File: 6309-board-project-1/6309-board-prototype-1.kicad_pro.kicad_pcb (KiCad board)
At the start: 2 copper layers, 100 x 140 mm, 35 parts, among them J1 PWR, J2 FTDI, SW1 B3F-1000, U1 63C09, U2 62256, U3 39FS010, U4 16550, U5 74HCT04, U6 74HCT32, U7 74HCT30, X1 12MHz, X2 1.8432 MHz

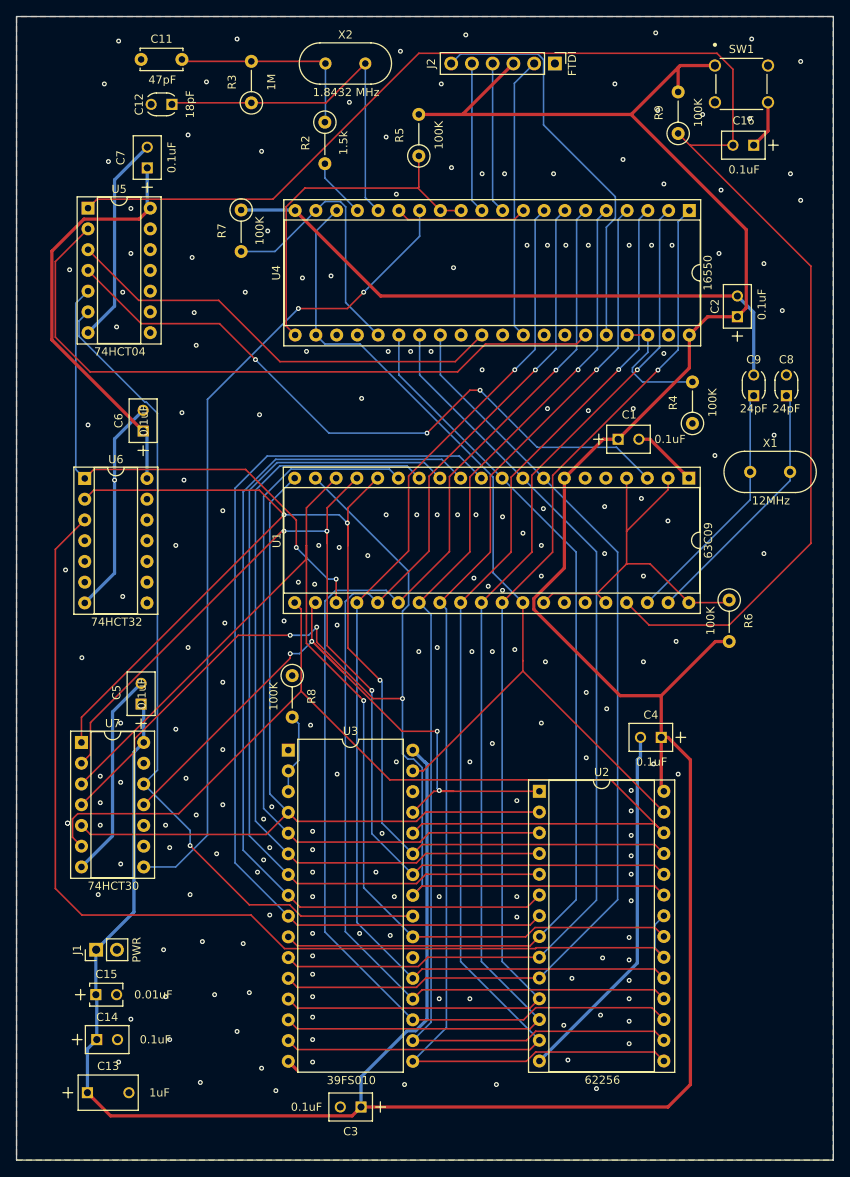
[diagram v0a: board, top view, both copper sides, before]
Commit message: remove excess vias
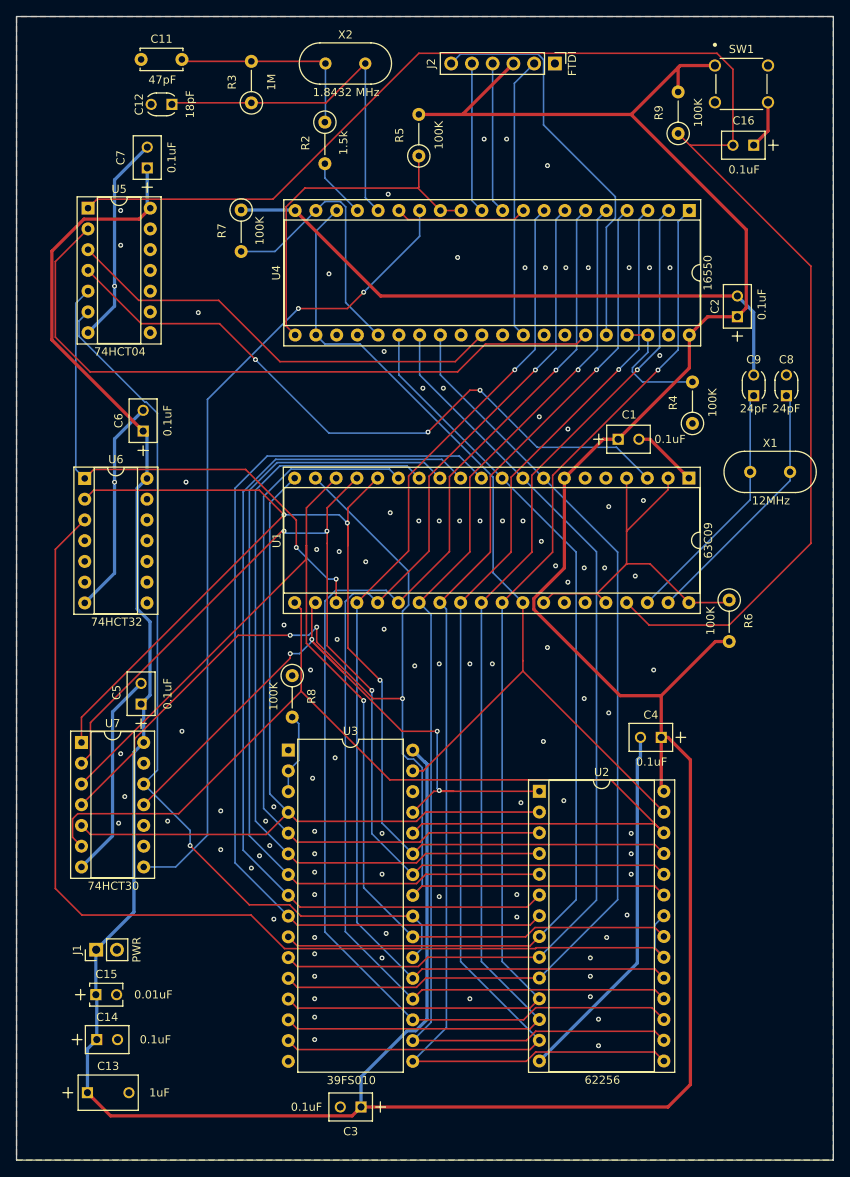
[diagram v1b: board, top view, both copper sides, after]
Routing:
- net +5V: track 446.2 -> 475.4 mm
- net /!A15: track 103.8 -> 109.8 mm
- net GND: track 213.7 -> 212.2 mm, vias 201 -> 101
- net /A9: track 131.7 -> 130.4 mm
- net /A5: vias 0 -> 1

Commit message: fix DRC errors
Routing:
- net /A14: track 85.1 -> 86.3 mm
- net GND: vias 101 -> 105
- net /A5: vias 1 -> 0
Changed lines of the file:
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@@
+	)
+	(via
+		(at 58.75 97.25)
+		(size 0.6)
+		(drill 0.3)
+		(layers "F.Cu" "B.Cu")
+		(free yes)
+		(net 2)
 	)
 	(via
@@
 	)
 	(via
+		(at 38.5 53)
+		(size 0.6)
+		(drill 0.3)
+		(layers "F.Cu" "B.Cu")
+		(free yes)
+		(net 2)
+	)
+	(via
 		(at 95.75 81.75)
 		(size 0.6)
@@
 	)
 	(via
+		(at 51.5 104)
+		(size 0.6)
+		(drill 0.3)
+		(layers "F.Cu" "B.Cu")
+		(free yes)
+		(net 2)
+	)
+	(via
 		(at 59 88.75)
 		(size 0.6)
@@
 		(drill 0.3)
 		(layers "F.Cu" "B.Cu")
+		(net 2)
+	)
+	(via
+		(at 46.75 92.5)
+		(size 0.6)
+		(drill 0.3)
+		(layers "F.Cu" "B.Cu")
+		(free yes)
 		(net 2)
 	)
@@
 		(net 18)
 	)
-	(via
-		(at 59.485 119.265)
-		(size 0.6)
-		(drill 0.3)
-		(layers "F.Cu" "B.Cu")
-		(net 18)
-	)
 	(segment
 		(start 59.485 119.265)
@@
 	)
 	(segment
+		(start 57.75 92.25)
+		(end 46.25 103.75)
+		(width 0.2)
+		(layer "F.Cu")
+		(net 32)
+	)
+	(segment
 		(start 78.1 109.1)
 		(end 79.75 109.1)
@@
 	)
 	(segment
+		(start 59.75 92.25)
+		(end 57.75 92.25)
+		(width 0.2)
+		(layer "F.Cu")
+		(net 32)
+	)
+	(segment
 		(start 78 109)
 		(end 78.1 109.1)
@@
 	)
 	(segment
-		(start 59.75 92.815)
-		(end 59.75 92.25)
-		(width 0.2)
-		(layer "F.Cu")
-		(net 32)
-	)
-	(segment
 		(start 74.76 111.68)
 		(end 77.34 109.1)
@@
 	)
 	(segment
+		(start 46.25 106.315)
+		(end 41.82 110.745)
+		(width 0.2)
+		(layer "F.Cu")
+		(net 32)
+	)
+	(segment
+		(start 46.25 103.75)
+		(end 46.25 106.315)
+		(width 0.2)
+		(layer "F.Cu")
+		(net 32)
+	)
+	(segment
 		(start 62.4 86.44)
 		(end 62.4 90.5)
@@
 		(width 0.2)
 		(layer "F.Cu")
-		(net 32)
-	)
-	(segment
-		(start 41.82 110.745)
-		(end 59.75 92.815)
-		(width 0.2)
-		(layer "F.Cu")

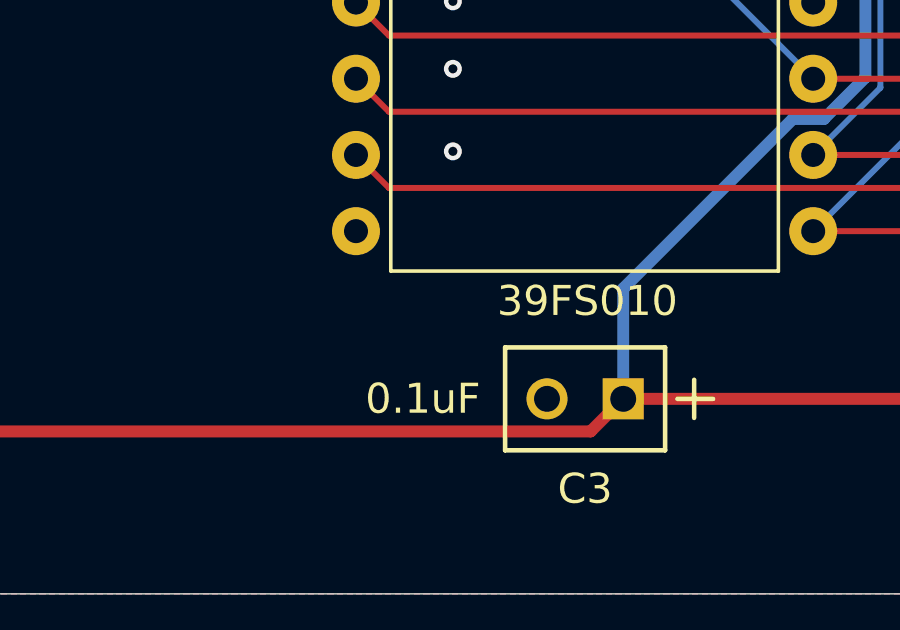
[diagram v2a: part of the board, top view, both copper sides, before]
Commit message: add ground connection to decoupling cap
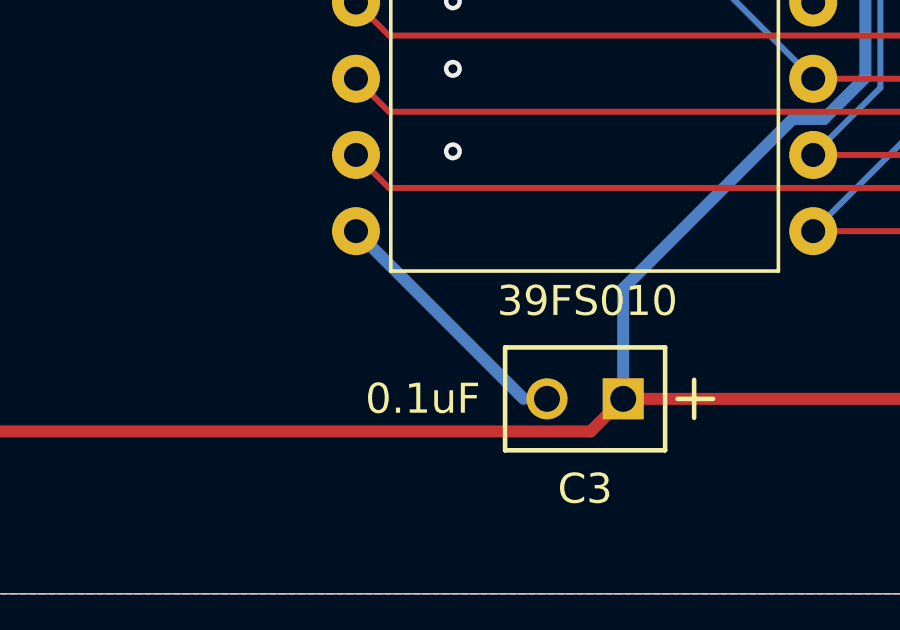
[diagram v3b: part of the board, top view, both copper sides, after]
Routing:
- net GND: track 212.2 -> 220.9 mm
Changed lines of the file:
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@@
+	)
+	(segment
+		(start 59.52 142.16)
+		(end 65.11 147.75)
+		(width 0.4)
+		(layer "B.Cu")
+		(net 2)
 	)
 	(segment
@@
 		(layer "B.Cu")
 		(net 2)
+	)
+	(segment
+		(start 65.11 147.75)
+		(end 65.8871 147.75)
+		(width 0.2)
+		(layer "B.Cu")
+		(net 2)
